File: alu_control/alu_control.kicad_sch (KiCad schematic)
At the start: 48 parts

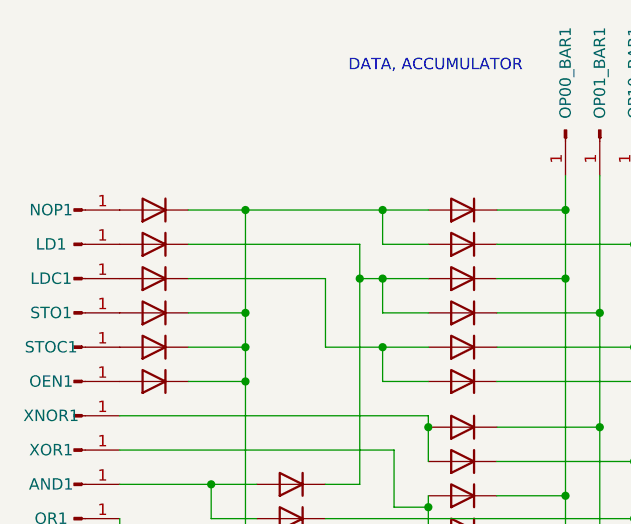
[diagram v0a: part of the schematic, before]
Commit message: Fix missing instruction on rom
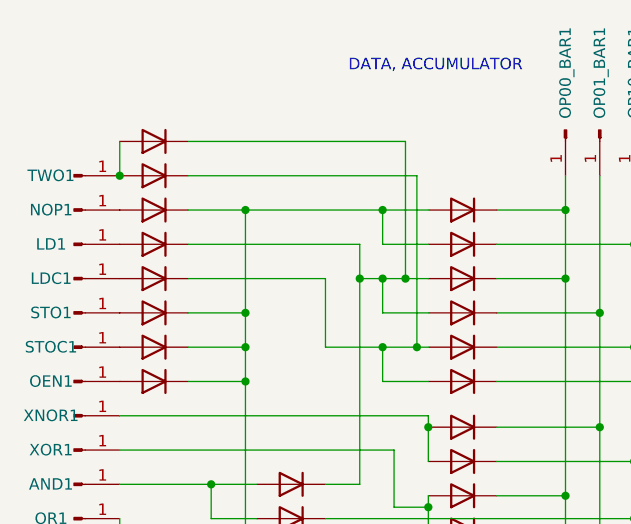
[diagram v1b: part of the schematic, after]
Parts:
- added D27, D28: D, Diode_THT:D_DO-34_SOD68_P7.62mm_Horizontal, symbol Device:D
- added TWO1: Conn_01x01_Pin, Connector_PinHeader_2.54mm:PinHeader_1x01_P2.54mm_Vertical, symbol Connector:Conn_01x01_Pin
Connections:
- net at D10.2 (A), D11.2 (A), D14.1 (K)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: now also D28.1 (K)
- net at D12.2 (A), D13.2 (A), D15.1 (K): now also D27.1 (K)
- new net: D27.2 (A), D28.2 (A), TWO1.1 (Pin_1)
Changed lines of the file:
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@@
   (junction (at 110.49 54.61) (diameter 0) (color 0 0 0 0)
   )
+  (junction (at 113.03 46.99) (diameter 0) (color 0 0 0 0)
+  )
   (junction (at 138.43 73.66) (diameter 0) (color 0 0 0 0)
   )
+  (junction (at 114.3 54.61) (diameter 0) (color 0 0 0 0)
+  )
   (junction (at 134.62 63.5) (diameter 0) (color 0 0 0 0)
   )
   (junction (at 115.57 63.5) (diameter 0) (color 0 0 0 0)
   )
+  (junction (at 81.28 35.56) (diameter 0) (color 0 0 0 0)
+  )
   (junction (at 142.24 74.93) (diameter 0) (color 0 0 0 0)
   )
@@
     (stroke (width 0) (type default))
   )
+  (wire (pts (xy 114.3 54.61) (xy 114.3 35.56))
+    (stroke (width 0) (type default))
+  )
   (wire (pts (xy 115.57 39.37) (xy 110.49 39.37))
     (stroke (width 0) (type default))
@@
     (stroke (width 0) (type default))
   )
+  (wire (pts (xy 113.03 46.99) (xy 115.57 46.99))
+    (stroke (width 0) (type default))
+  )
   (wire (pts (xy 115.57 63.5) (xy 115.57 67.31))
     (stroke (width 0) (type default))
@@
     (stroke (width 0) (type default))
   )
+  (wire (pts (xy 113.03 31.75) (xy 88.9 31.75))
+    (stroke (width 0) (type default))
+  )
   (wire (pts (xy 91.44 73.66) (xy 91.44 69.85))
     (stroke (width 0) (type default))
@@
     (stroke (width 0) (type default))
   )
+  (wire (pts (xy 113.03 46.99) (xy 113.03 31.75))
+    (stroke (width 0) (type default))
+  )
   (wire (pts (xy 123.19 58.42) (xy 142.24 58.42))
     (stroke (width 0) (type default))
@@
     (stroke (width 0) (type default))
   )
-  (wire (pts (xy 115.57 54.61) (xy 110.49 54.61))
-    (stroke (width 0) (type default))
-  )
-  (wire (pts (xy 110.49 46.99) (xy 115.57 46.99))
+  (wire (pts (xy 115.57 54.61) (xy 114.3 54.61))
+    (stroke (width 0) (type default))
+  )
+  (wire (pts (xy 110.49 46.99) (xy 113.03 46.99))
     (stroke (width 0) (type default))
   )
@@
     (stroke (width 0) (type default))
   )
+  (wire (pts (xy 114.3 54.61) (xy 110.49 54.61))
+    (stroke (width 0) (type default))
+  )
   (wire (pts (xy 104.14 54.61) (xy 110.49 54.61))
     (stroke (width 0) (type default))
   )
+  (wire (pts (xy 114.3 35.56) (xy 88.9 35.56))
+    (stroke (width 0) (type default))
+  )
   (wire (pts (xy 110.49 39.37) (xy 95.25 39.37))
     (stroke (width 0) (type default))
@@
   )
   (wire (pts (xy 123.19 71.12) (xy 130.81 71.12))
+    (stroke (width 0) (type default))
+  )
+  (wire (pts (xy 81.28 31.75) (xy 81.28 35.56))
     (stroke (width 0) (type default))
   )
@@
     )
   )
+  (symbol (lib_id "Connector:Conn_01x01_Pin") (at 76.2 35.56 0) (unit 1)
+    (in_bom yes) (on_board yes) (dnp no)
+    (property "Reference" "TWO1" (at 73.66 35.56 0)
+      (effects (font (size 1.27 1.27)))
+    )
+    (property "Value" "Conn_01x01_Pin" (at 76.835 33.02 0)
+      (effects (font (size 1.27 1.27)) hide)
+    )
+    (property "Footprint" "Connector_PinHeader_2.54mm:PinHeader_1x01_P2.54mm_Vertical" (at 76.2 35.56 0)
+      (effects (font (size 1.27 1.27)) hide)
+    )
+    (property "Datasheet" "~" (at 76.2 35.56 0)
+      (effects (font (size 1.27 1.27)) hide)
+    )
+    (pin "1")
+    (instances
+      (project "alu_control"
+        (path "/ae00940c-1f3d-4df8-b652-63503ec25af3"
+          (reference "TWO1") (unit 1)
+        )
+      )
+    )
+  )
   (symbol (lib_id "Device:R_US") (at 138.43 82.55 0) (unit 1)
     (in_bom yes) (on_board yes) (dnp no) (fields_autoplaced)
@@
     )
   )
+  (symbol (lib_id "Device:D") (at 85.09 31.75 180) (unit 1)
+    (in_bom yes) (on_board yes) (dnp no)
+    (property "Reference" "D28" (at 85.09 29.21 0)
+      (effects (font (size 1.27 1.27)) hide)
+    )
+    (property "Value" "D" (at 85.09 27.94 0)
+      (effects (font (size 1.27 1.27)) hide)
+    )
+    (property "Footprint" "Diode_THT:D_DO-34_SOD68_P7.62mm_Horizontal" (at 85.09 31.75 0)
+      (effects (font (size 1.27 1.27)) hide)
+    )
+    (property "Datasheet" "~" (at 85.09 31.75 0)
+      (effects (font (size 1.27 1.27)) hide)
+    )
+    (property "Sim.Device" "D" (at 85.09 31.75 0)
+      (effects (font (size 1.27 1.27)) hide)
+    )
+    (property "Sim.Pins" "1=K 2=A" (at 85.09 31.75 0)
+      (effects (font (size 1.27 1.27)) hide)
+    )
+    (pin "1")
+    (pin "2")
+    (instances
+      (project "alu_control"
+        (path "/ae00940c-1f3d-4df8-b652-63503ec25af3"
+          (reference "D28") (unit 1)
+        )
+      )
+    )
+  )
   (symbol (lib_id "Connector:Conn_01x01_Pin") (at 76.2 43.18 0) (unit 1)
     (in_bom yes) (on_board yes) (dnp no)
@@
         )
       )
+    )
+  )
+  (symbol (lib_id "Device:D") (at 85.09 35.56 180) (unit 1)
+    (in_bom yes) (on_board yes) (dnp no)
+    (property "Reference" "D27" (at 85.09 33.02 0)
+      (effects (font (size 1.27 1.27)) hide)
+    )
+    (property "Value" "D" (at 85.09 31.75 0)
+      (effects (font (size 1.27 1.27)) hide)
+    )
+    (property "Footprint" "Diode_THT:D_DO-34_SOD68_P7.62mm_Horizontal" (at 85.09 35.56 0)
+      (effects (font (size 1.27 1.27)) hide)
+    )
+    (property "Datasheet" "~" (at 85.09 35.56 0)
+      (effects (font (size 1.27 1.27)) hide)
+    )
+    (property "Sim.Device" "D" (at 85.09 35.56 0)
+      (effects (font (size 1.27 1.27)) hide)
+    )
+    (property "Sim.Pins" "1=K 2=A" (at 85.09 35.56 0)
+      (effects (font (size 1.27 1.27)) hide)
+    )
+    (pin "1")
+    (pin "2")
+    (instances
+      (project "alu_control"
+        (path "/ae00940c-1f3d-4df8-b652-63503ec25af3"
+          (reference "D27") (unit 1)
+        )
+      )

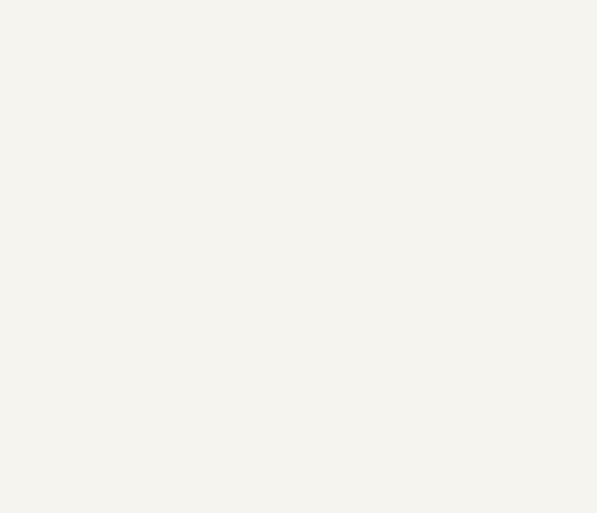
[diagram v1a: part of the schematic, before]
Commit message: add logic unit, fix control
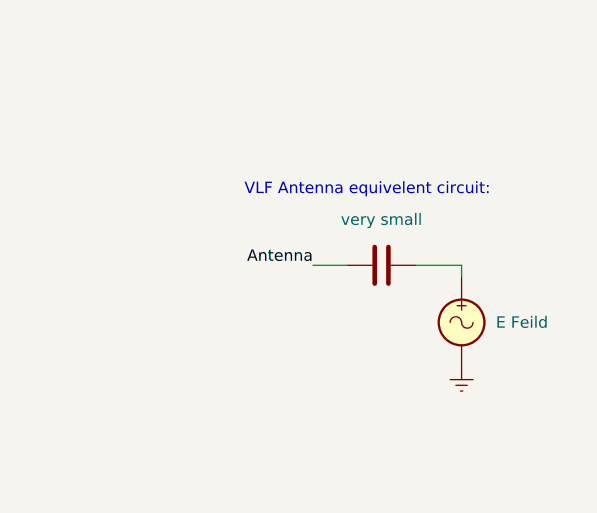
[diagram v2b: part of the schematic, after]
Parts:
- added C1: very small, symbol Device:C
- added V1: E Feild, symbol Simulation_SPICE:VSIN
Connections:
- new net: C1.2, V1.1
- new net Antenna: C1.1
- new net Earth: V1.2
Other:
- note added: "VLF Antenna equivelent circuit:"
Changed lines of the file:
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@@
+    (stroke (width 0) (type default))
+  )
+  (wire (pts (xy 229.87 95.25) (xy 229.87 93.98))
     (stroke (width 0) (type default))
   )
@@
     (stroke (width 0) (type default))
   )
+  (wire (pts (xy 224.79 93.98) (xy 229.87 93.98))
+    (stroke (width 0) (type default))
+  )
   (wire (pts (xy 130.81 46.99) (xy 130.81 71.12))
     (stroke (width 0) (type default))
@@
   )
   (wire (pts (xy 110.49 50.8) (xy 110.49 46.99))
+    (stroke (width 0) (type default))
+  )
+  (wire (pts (xy 213.36 93.98) (xy 217.17 93.98))
     (stroke (width 0) (type default))
   )
@@
   (text "DATA, ACCUMULATOR" (at 106.68 24.13 0)
     (effects (font (size 1.27 1.27)) (justify left bottom))
+  )
+  (text "VLF Antenna equivelent circuit:" (at 205.74 86.36 0)
+    (effects (font (size 1.27 1.27)) (justify left bottom))
+  )
+  (label "Antenna" (at 213.36 93.98 180) (fields_autoplaced)
+    (effects (font (size 1.27 1.27)) (justify right bottom))
   )
   (symbol (lib_id "Device:LED") (at 130.81 90.17 90) (unit 1)
@@
     )
   )
+  (symbol (lib_id "Device:C") (at 220.98 93.98 90) (unit 1)
+    (in_bom yes) (on_board yes) (dnp no) (fields_autoplaced)
+    (property "Reference" "C1" (at 220.98 86.36 90)
+      (effects (font (size 1.27 1.27)) hide)
+    )
+    (property "Value" "very small" (at 220.98 88.9 90)
+      (effects (font (size 1.27 1.27)))
+    )
+    (property "Footprint" "" (at 224.79 93.0148 0)
+      (effects (font (size 1.27 1.27)) hide)
+    )
+    (property "Datasheet" "~" (at 220.98 93.98 0)
+      (effects (font (size 1.27 1.27)) hide)
+    )
+    (pin "1")
+    (pin "2")
+    (instances
+      (project "alu_control"
+        (path "/ae00940c-1f3d-4df8-b652-63503ec25af3"
+          (reference "C1") (unit 1)
+        )
+      )
+    )
+  )
   (symbol (lib_id "Device:LED") (at 142.24 90.17 90) (unit 1)
     (in_bom yes) (on_board yes) (dnp no)
@@
     )
   )
+  (symbol (lib_id "power:Earth") (at 229.87 105.41 0) (unit 1)
+    (in_bom yes) (on_board yes) (dnp no) (fields_autoplaced)
+    (property "Reference" "#PWR06" (at 229.87 111.76 0)
+      (effects (font (size 1.27 1.27)) hide)
+    )
+    (property "Value" "Earth" (at 229.87 109.22 0)
+      (effects (font (size 1.27 1.27)) hide)
+    )
+    (property "Footprint" "" (at 229.87 105.41 0)
+      (effects (font (size 1.27 1.27)) hide)
+    )
+    (property "Datasheet" "~" (at 229.87 105.41 0)
+      (effects (font (size 1.27 1.27)) hide)
+    )
+    (pin "1")
+    (instances
+      (project "alu_control"
+        (path "/ae00940c-1f3d-4df8-b652-63503ec25af3"
+          (reference "#PWR06") (unit 1)
+        )
+      )
+    )
+  )
   (symbol (lib_id "Connector:Conn_01x01_Pin") (at 76.2 66.04 0) (unit 1)
     (in_bom yes) (on_board yes) (dnp no)
@@
         )
       )
+    )
+  )
+  (symbol (lib_id "Simulation_SPICE:VSIN") (at 229.87 100.33 0) (unit 1)
+    (in_bom yes) (on_board yes) (dnp no)
+    (property "Reference" "V1" (at 233.68 98.9302 0)
+      (effects (font (size 1.27 1.27)) (justify left) hide)
+    )
+    (property "Value" "E Feild" (at 233.68 100.33 0)
+      (effects (font (size 1.27 1.27)) (justify left))
+    )
+    (property "Footprint" "" (at 229.87 100.33 0)
+      (effects (font (size 1.27 1.27)) hide)
+    )
+    (property "Datasheet" "~" (at 229.87 100.33 0)
+      (effects (font (size 1.27 1.27)) hide)
+    )
+    (property "Sim.Pins" "1=+ 2=-" (at 229.87 100.33 0)
+      (effects (font (size 1.27 1.27)) hide)
+    )
+    (property "Sim.Params" "dc=0 ampl=1 f=1k ac=1" (at 233.68 102.7402 0)
+      (effects (font (size 1.27 1.27)) (justify left) hide)
+    )
+    (property "Sim.Type" "SIN" (at 229.87 100.33 0)
+      (effects (font (size 1.27 1.27)) hide)
+    )
+    (property "Sim.Device" "V" (at 229.87 100.33 0)
+      (effects (font (size 1.27 1.27)) (justify left) hide)
+    )
+    (pin "1")
+    (pin "2")
+    (instances
+      (project "alu_control"
+        (path "/ae00940c-1f3d-4df8-b652-63503ec25af3"
+          (reference "V1") (unit 1)
+        )
+      )
